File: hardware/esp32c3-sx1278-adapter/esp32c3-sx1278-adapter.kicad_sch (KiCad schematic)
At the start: 5 parts, among them J1 Conn_01x08, J2 Conn_01x08, J3 Antenna, J4 SMA, U2 SX1278_module

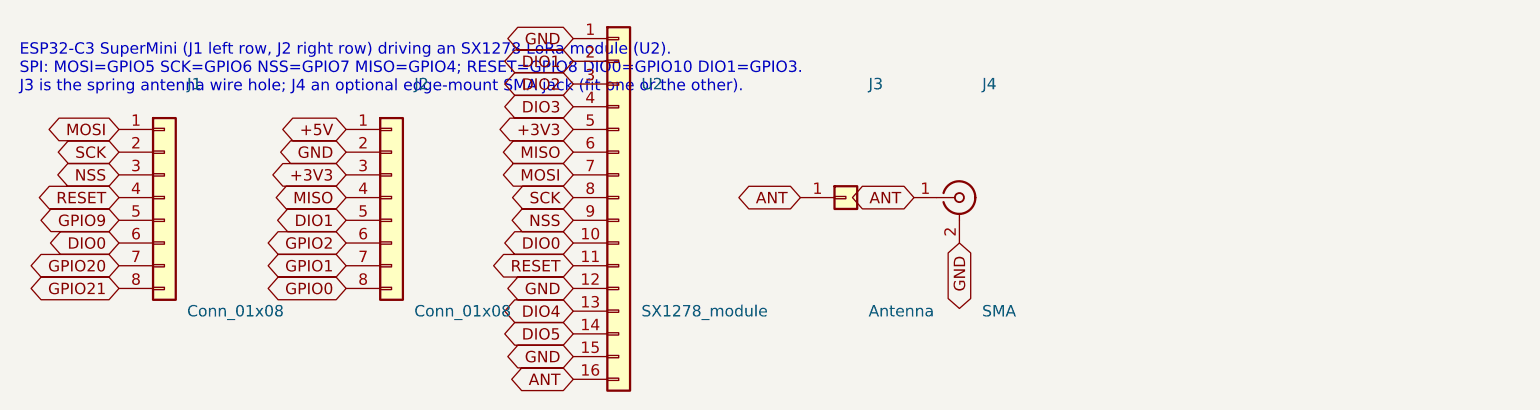
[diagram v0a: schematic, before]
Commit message: Adapters: expansion header for the unused SuperMini pins and a radio-type strap
Pin-header adapter:
* J4, a 1x7 2.54 mm header on the top edge, carries every SuperMini pin the
  radio does not use: 5V, GPIO8, GPIO9, GPIO2, GPIO20, GPIO21, GPIO0.  Its
  pins sit at the gaps between the SuperMini's pins so each net reaches it on
  the front copper without crossing another (power-row nets jog above their
  row, GPIO-row nets rise between the rows and pass between the power-row
  pads).  The radio tracks on the back are unchanged; the GND pour flows
  around the new tracks.
* JP1, a two-pad solder jumper right of the SuperMini, straps GPIO1 (net
  RADIO_ID) to GND: open = CC1101 E07-M1101D, bridged = Ra-02 breakout.

SX1278 module adapter: GPIO1 is tied to 3V3 (silk "ID=3V3"), so the same
pin reads high there.  Firmware samples GPIO1 with the internal pull-down
and then the pull-up to tell the three states apart; GPIO1 is not a boot
strapping pin.

The header is 2.3 mm from the top edge so the MISO lane on the back keeps
its clearance under it.  Both adapters pass ERC and DRC; README and the
manufacturing notes describe the header and the strap.

Co-Authored-By: Claude Fable 5.1 <noreply@anthropic.com>
Claude-Session: https://claude.ai/code/session_01JoGdh4Cg3VtTTDZi4gQuiN
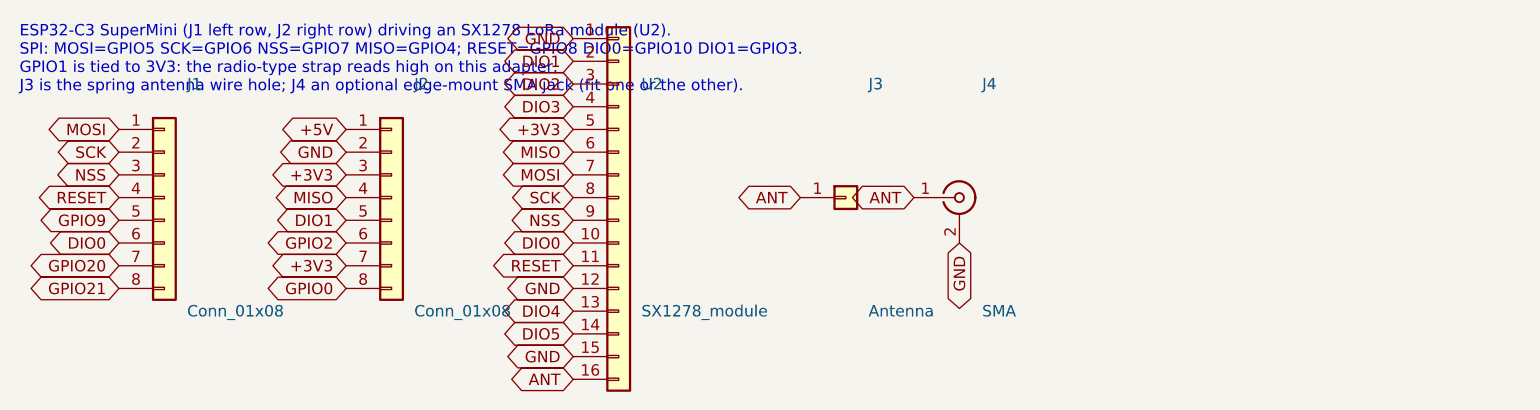
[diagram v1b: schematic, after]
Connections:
- net GPIO1 is gone; now on net +3V3: J2.7 (Pin_7)
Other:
- note added: "ESP32-C3 SuperMini (J1 left row, J2 right row) driving an SX1278 LoRa module (U2). SPI: MOSI=GPIO5 SCK=GPIO6 NSS=GPIO7 MISO=GPIO4; RESET=GPIO8 DIO0=GPIO10 DIO1=GPIO3. GPIO1 is tied to 3V3: the radio-type strap reads high on this adapter. J3 is the spring antenna wire hole; J4 an optional edge-mount SMA jack (fit one or the other)."
- note removed: "ESP32-C3 SuperMini (J1 left row, J2 right row) driving an SX1278 LoRa module (U2). SPI: MOSI=GPIO5 SCK=GPIO6 NSS=GPIO7 MISO=GPIO4; RESET=GPIO8 DIO0=GPIO10 DIO1=GPIO3. J3 is the spring antenna wire hole; J4 an optional edge-mount SMA jack (fit one or the other)."
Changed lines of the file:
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@@
 		)
 	)
-	(global_label "GPIO1"
+	(global_label "+3V3"
 		(shape bidirectional)
 		(at 96.52 109.22 180)
@@
 		)
 	)
-	(text "ESP32-C3 SuperMini (J1 left row, J2 right row) driving an SX1278 LoRa module (U2).\nSPI: MOSI=GPIO5 SCK=GPIO6 NSS=GPIO7 MISO=GPIO4; RESET=GPIO8 DIO0=GPIO10 DIO1=GPIO3.\nJ3 is the spring antenna wire hole; J4 an optional edge-mount SMA jack (fit one or the other)."
+	(text "ESP32-C3 SuperMini (J1 left row, J2 right row) driving an SX1278 LoRa module (U2).\nSPI: MOSI=GPIO5 SCK=GPIO6 NSS=GPIO7 MISO=GPIO4; RESET=GPIO8 DIO0=GPIO10 DIO1=GPIO3.\nGPIO1 is tied to 3V3: the radio-type strap reads high on this adapter.\nJ3 is the spring antenna wire hole; J4 an optional edge-mount SMA jack (fit one or the other)."
 		(exclude_from_sim no)
 		(at 60 90 0)

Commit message: Adapters: reassign the GPIOs so the socket adapter routes on one layer
The pin-header (socket) adapter is now entirely on the back copper, the
expansion header and strap included; the front carries only pads and the
GND pour.  New assignment, shared by both adapters:

  MOSI GPIO8, SCK GPIO9, CSN/NSS GPIO0, MISO GPIO7, GDO0/RST(DIO0) GPIO10,
  GDO2/DIO0(DIO1) GPIO6, strap RADIO_ID GPIO5, SX1278 module RESET GPIO4.

GPIO8/9 are boot strapping pins but carry only ESP32 outputs, which float
at boot; the radio's outputs stay on plain GPIOs.  On the socket adapter
the radio signals then all leave the GPIO row, which faces the socket, in
the order its pads want them: GDO0 and SCK drop straight in, MOSI and MISO
via one lane each, GDO2 round the left of the socket into its pad from
below.  CSN/NSS (GPIO0, the last power-row pin) passes under its own pad,
crosses between the rows (now otherwise empty) and drops through a
GPIO-row gap.  GND and 3V3 leave the power row upward, run along the top
edge above the header and down the strip right of the SuperMini into the
socket's right column; GND continues under the socket to the strap.

Expansion header J4 (centred): 3V3, GPIO4, 3, 2, 1, 21, 20 - GPIO4..1 rise
straight up, GPIO21/20 come up the right-hand strip.  5V is dropped: its
pad sits under the top-left hole and cannot be reached on one layer.  The
strap moves to the bottom-left corner (JP1 header, R1 0805 on the back),
fed by GPIO5 dropping straight down and by the under-socket GND lane.

SX1278 module adapter: same map; its GPIO order matches the module's pad
order so the front-copper lanes stay nested; NSS and RESET now come from
the right column on the back copper, 3V3 goes down the right of the
SuperMini, and GPIO5 is tied to 3V3 across the top.

Both adapters pass ERC and DRC; the antenna keepout starts 1.6 mm inboard
of the power row (was 1.3) to give CSN/NSS its lane under the last pad.

Co-Authored-By: Claude Fable 5.1 <noreply@anthropic.com>
Claude-Session: https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
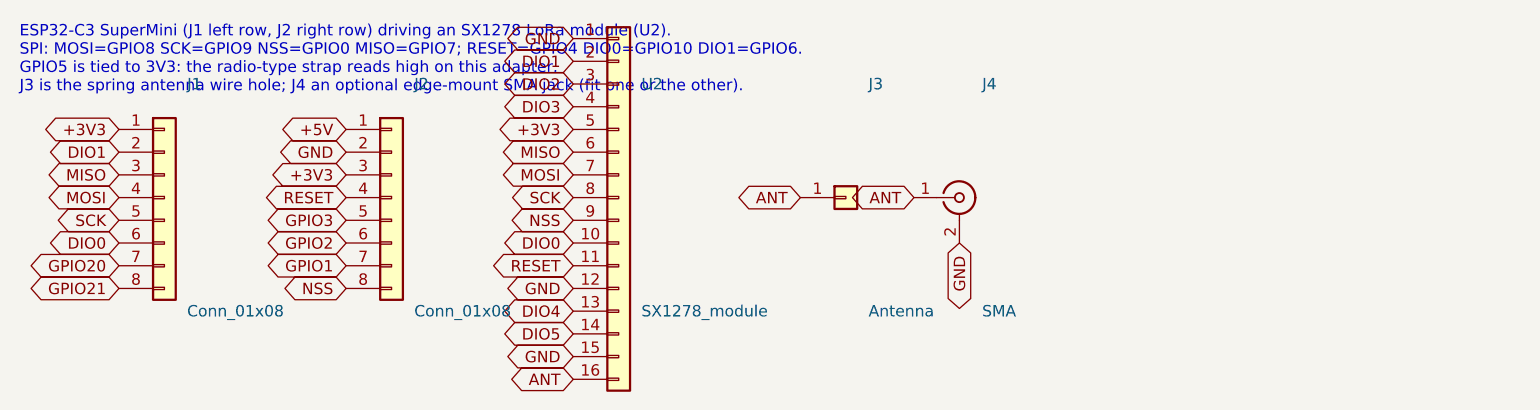
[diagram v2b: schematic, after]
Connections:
- net GPIO0 is gone; now on net NSS: J2.8 (Pin_8)
- net GPIO9 is gone; now on net SCK: J1.5 (Pin_5)
- net +3V3: now also J1.1 (Pin_1); no longer J2.7 (Pin_7)
- net DIO1: now also J1.2 (Pin_2); no longer J2.5 (Pin_5)
- net MISO: now also J1.3 (Pin_3); no longer J2.4 (Pin_4)
- net MOSI: now also J1.4 (Pin_4); no longer J1.1 (Pin_1)
- net NSS: no longer J1.3 (Pin_3)
- net RESET: now also J2.4 (Pin_4); no longer J1.4 (Pin_4)
- net SCK: no longer J1.2 (Pin_2)
- new net GPIO1: J2.7 (Pin_7)
- new net GPIO3: J2.5 (Pin_5)
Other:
- note added: "ESP32-C3 SuperMini (J1 left row, J2 right row) driving an SX1278 LoRa module (U2). SPI: MOSI=GPIO8 SCK=GPIO9 NSS=GPIO0 MISO=GPIO7; RESET=GPIO4 DIO0=GPIO10 DIO1=GPIO6. GPIO5 is tied to 3V3: the radio-type strap reads high on this adapter. J3 is the spring antenna wire hole; J4 an optional edge-mount SMA jack (fit one or the other)."
- note removed: "ESP32-C3 SuperMini (J1 left row, J2 right row) driving an SX1278 LoRa module (U2). SPI: MOSI=GPIO5 SCK=GPIO6 NSS=GPIO7 MISO=GPIO4; RESET=GPIO8 DIO0=GPIO10 DIO1=GPIO3. GPIO1 is tied to 3V3: the radio-type strap reads high on this adapter. J3 is the spring antenna wire hole; J4 an optional edge-mount SMA jack (fit one or the other)."
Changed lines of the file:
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@@
+		)
+	)
+	(global_label "+3V3"
+		(shape bidirectional)
+		(at 71.12 93.98 180)
+		(fields_autoplaced yes)
+		(effects
+			(font
+				(size 1.27 1.27)
+			)
+			(justify right)
+		)
+		(property "Intersheetrefs" "${INTERSHEET_REFS}"
+			(at 71.12 93.98 0)
+			(effects
+				(font
+					(size 1.27 1.27)
+				)
+				(justify right)
+				(hide yes)
+			)
+		)
+	)
+	(global_label "DIO1"
+		(shape bidirectional)
+		(at 71.12 96.52 180)
+		(fields_autoplaced yes)
+		(effects
+			(font
+				(size 1.27 1.27)
+			)
+			(justify right)
+		)
+		(property "Intersheetrefs" "${INTERSHEET_REFS}"
+			(at 71.12 96.52 0)
+			(effects
+				(font
+					(size 1.27 1.27)
+				)
+				(justify right)
+				(hide yes)
+			)
+		)
+	)
+	(global_label "MISO"
+		(shape bidirectional)
+		(at 71.12 99.06 180)
+		(fields_autoplaced yes)
+		(effects
+			(font
+				(size 1.27 1.27)
+			)
+			(justify right)
+		)
+		(property "Intersheetrefs" "${INTERSHEET_REFS}"
+			(at 71.12 99.06 0)
+			(effects
+				(font
+					(size 1.27 1.27)
+				)
+				(justify right)
+				(hide yes)
+			)
 		)
 	)
 	(global_label "MOSI"
 		(shape bidirectional)
-		(at 71.12 93.98 180)
-		(fields_autoplaced yes)
-		(effects
-			(font
-				(size 1.27 1.27)
-			)
-			(justify right)
-		)
-		(property "Intersheetrefs" "${INTERSHEET_REFS}"
-			(at 71.12 93.98 0)
+		(at 71.12 101.6 180)
+		(fields_autoplaced yes)
+		(effects
+			(font
+				(size 1.27 1.27)
+			)
+			(justify right)
+		)
+		(property "Intersheetrefs" "${INTERSHEET_REFS}"
+			(at 71.12 101.6 0)
 			(effects
 				(font
@@
 	)
 	(global_label "SCK"
-		(shape bidirectional)
-		(at 71.12 96.52 180)
-		(fields_autoplaced yes)
-		(effects
-			(font
-				(size 1.27 1.27)
-			)
-			(justify right)
-		)
-		(property "Intersheetrefs" "${INTERSHEET_REFS}"
-			(at 71.12 96.52 0)
-			(effects
-				(font
-					(size 1.27 1.27)
-				)
-				(justify right)
-				(hide yes)
-			)
-		)
-	)
-	(global_label "NSS"
-		(shape bidirectional)
-		(at 71.12 99.06 180)
-		(fields_autoplaced yes)
-		(effects
-			(font
-				(size 1.27 1.27)
-			)
-			(justify right)
-		)
-		(property "Intersheetrefs" "${INTERSHEET_REFS}"
-			(at 71.12 99.06 0)
-			(effects
-				(font
-					(size 1.27 1.27)
-				)
-				(justify right)
-				(hide yes)
-			)
-		)
-	)
-	(global_label "RESET"
-		(shape bidirectional)
-		(at 71.12 101.6 180)
-		(fields_autoplaced yes)
-		(effects
-			(font
-				(size 1.27 1.27)
-			)
-			(justify right)
-		)
-		(property "Intersheetrefs" "${INTERSHEET_REFS}"
-			(at 71.12 101.6 0)
-			(effects
-				(font
-					(size 1.27 1.27)
-				)
-				(justify right)
-				(hide yes)
-			)
-		)
-	)
-	(global_label "GPIO9"
 		(shape bidirectional)
 		(at 71.12 104.14 180)
@@
 		)
 	)
-	(global_label "MISO"
+	(global_label "RESET"
 		(shape bidirectional)
 		(at 96.52 101.6 180)
@@
 		)
 	)
-	(global_label "DIO1"
+	(global_label "GPIO3"
 		(shape bidirectional)
 		(at 96.52 104.14 180)
@@
 		)
 	)
-	(global_label "+3V3"
+	(global_label "GPIO1"
 		(shape bidirectional)
 		(at 96.52 109.22 180)
@@
 		)
 	)
-	(global_label "GPIO0"
+	(global_label "NSS"
 		(shape bidirectional)
 		(at 96.52 111.76 180)
@@
 		)
 	)
-	(text "ESP32-C3 SuperMini (J1 left row, J2 right row) driving an SX1278 LoRa module (U2).\nSPI: MOSI=GPIO5 SCK=GPIO6 NSS=GPIO7 MISO=GPIO4; RESET=GPIO8 DIO0=GPIO10 DIO1=GPIO3.\nGPIO1 is tied to 3V3: the radio-type strap reads high on this adapter.\nJ3 is the spring antenna wire hole; J4 an optional edge-mount SMA jack (fit one or the other)."
+	(text "ESP32-C3 SuperMini (J1 left row, J2 right row) driving an SX1278 LoRa module (U2).\nSPI: MOSI=GPIO8 SCK=GPIO9 NSS=GPIO0 MISO=GPIO7; RESET=GPIO4 DIO0=GPIO10 DIO1=GPIO6.\nGPIO5 is tied to 3V3: the radio-type strap reads high on this adapter.\nJ3 is the spring antenna wire hole; J4 an optional edge-mount SMA jack (fit one or the other)."
 		(exclude_from_sim no)
 		(at 60 90 0)

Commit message: Adapters: GPIO map that lets the same socket take all three radio boards
The green D-Sun CC1101 board plugs into the socket adapter's 2x4 socket
too; only its signal order differs, which the firmware absorbs with a pin
map per board.  What the hardware must guarantee is that no socket
position that carries a radio OUTPUT on any of the boards is an ESP32-C3
boot strapping pin (GPIO2/8/9).  Only position 4 (blue CSN, green SCK,
Ra-02 NSS) is an input on every board, so it takes GPIO9; GPIO8 moves to
the spare header and positions 5 and 6 are fed from GPIO3 and GPIO4.

Socket positions 3..8 are now GPIO10, 9, 3, 4, 7, 6.  Per-board maps:
blue E07 MOSI 4 SCK 3 CSN 9 MISO 7 GDO0 10 GDO2 6; green D-Sun MOSI 10
SCK 9 CSN 6 MISO 3 GDO0 7 GDO2 4; Ra-02 MOSI 4 SCK 3 NSS 9 MISO 7 RST 10
DIO0 6.  The README also describes telling the two CC1101 boards apart
passively at power-up (an unconfigured CC1101 clocks XOSC/192 out of
GDO0, on GPIO10 for the blue board and GPIO7 for the green).

Socket adapter routing, still entirely on the back copper: GPIO9 leaves
its pad sideways into the gap before GPIO10 and drops into position 4;
MISO takes the column under GPIO8's pad; SCK and MOSI come down from the
power row through the gaps either side of GPIO8's pad, and GPIO8 climbs
between them to the header (now 3V3, 8, 2, 1, 0, 21TX, 20RX).

SX1278 module adapter: same GPIOs with MOSI and SCK swapped (GPIO3/4) so
its bottom copper nests, NSS on GPIO9 via the top-copper bus, RESET on
GPIO8 (an ESP32 output).

Jumper-wire diagrams: one layout serves all three boards; GPIO4 and GPIO3
take the ribbon's white and black; the Ra-02 strap goes to GPIO1 (GPIO4
is now MOSI).  Both adapters pass ERC and DRC.

Co-Authored-By: Claude Fable 5.1 <noreply@anthropic.com>
Claude-Session: https://claude.ai/code/session_01JoGdh4Cg3VtTTDZi4gQuiN
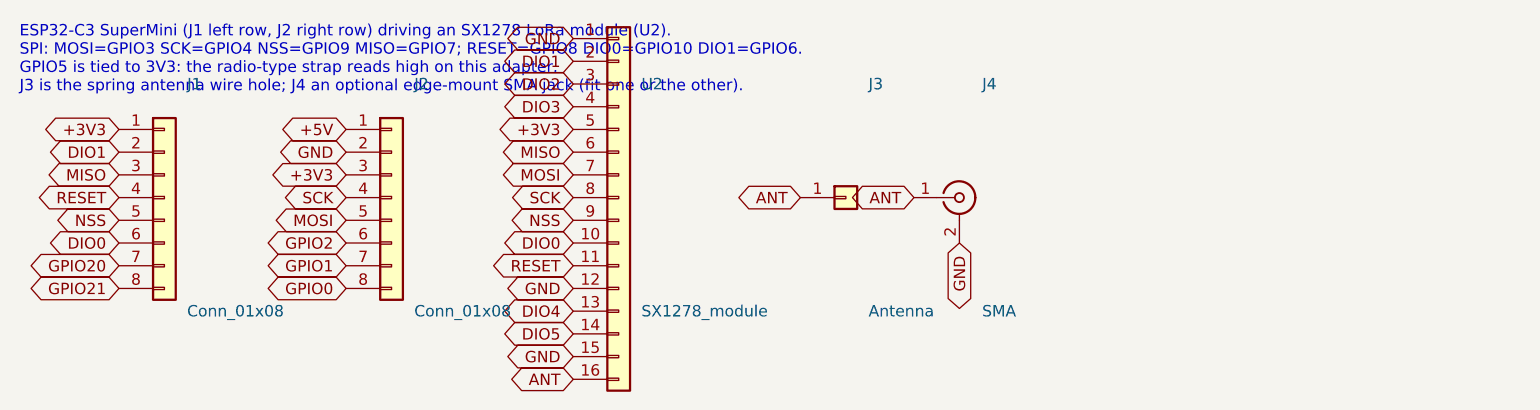
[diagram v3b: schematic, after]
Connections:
- net GPIO3 is gone; now on net MOSI: J2.5 (Pin_5)
- net MOSI: no longer J1.4 (Pin_4)
- net NSS: now also J1.5 (Pin_5); no longer J2.8 (Pin_8)
- net RESET: now also J1.4 (Pin_4); no longer J2.4 (Pin_4)
- net SCK: now also J2.4 (Pin_4); no longer J1.5 (Pin_5)
- new net GPIO0: J2.8 (Pin_8)
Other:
- note added: "ESP32-C3 SuperMini (J1 left row, J2 right row) driving an SX1278 LoRa module (U2). SPI: MOSI=GPIO3 SCK=GPIO4 NSS=GPIO9 MISO=GPIO7; RESET=GPIO8 DIO0=GPIO10 DIO1=GPIO6. GPIO5 is tied to 3V3: the radio-type strap reads high on this adapter. J3 is the spring antenna wire hole; J4 an optional edge-mount SMA jack (fit one or the other)."
- note removed: "ESP32-C3 SuperMini (J1 left row, J2 right row) driving an SX1278 LoRa module (U2). SPI: MOSI=GPIO8 SCK=GPIO9 NSS=GPIO0 MISO=GPIO7; RESET=GPIO4 DIO0=GPIO10 DIO1=GPIO6. GPIO5 is tied to 3V3: the radio-type strap reads high on this adapter. J3 is the spring antenna wire hole; J4 an optional edge-mount SMA jack (fit one or the other)."
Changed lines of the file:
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@@
 		)
 	)
-	(global_label "MOSI"
+	(global_label "RESET"
 		(shape bidirectional)
 		(at 71.12 101.6 180)
@@
 		)
 	)
-	(global_label "SCK"
+	(global_label "NSS"
 		(shape bidirectional)
 		(at 71.12 104.14 180)
@@
 		)
 	)
-	(global_label "RESET"
+	(global_label "SCK"
 		(shape bidirectional)
 		(at 96.52 101.6 180)
@@
 		)
 	)
-	(global_label "GPIO3"
+	(global_label "MOSI"
 		(shape bidirectional)
 		(at 96.52 104.14 180)
@@
 		)
 	)
-	(global_label "NSS"
+	(global_label "GPIO0"
 		(shape bidirectional)
 		(at 96.52 111.76 180)
@@
 		)
 	)
-	(text "ESP32-C3 SuperMini (J1 left row, J2 right row) driving an SX1278 LoRa module (U2).\nSPI: MOSI=GPIO8 SCK=GPIO9 NSS=GPIO0 MISO=GPIO7; RESET=GPIO4 DIO0=GPIO10 DIO1=GPIO6.\nGPIO5 is tied to 3V3: the radio-type strap reads high on this adapter.\nJ3 is the spring antenna wire hole; J4 an optional edge-mount SMA jack (fit one or the other)."
+	(text "ESP32-C3 SuperMini (J1 left row, J2 right row) driving an SX1278 LoRa module (U2).\nSPI: MOSI=GPIO3 SCK=GPIO4 NSS=GPIO9 MISO=GPIO7; RESET=GPIO8 DIO0=GPIO10 DIO1=GPIO6.\nGPIO5 is tied to 3V3: the radio-type strap reads high on this adapter.\nJ3 is the spring antenna wire hole; J4 an optional edge-mount SMA jack (fit one or the other)."
 		(exclude_from_sim no)
 		(at 60 90 0)
